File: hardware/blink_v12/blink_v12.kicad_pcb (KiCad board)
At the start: 2 copper layers, 119 x 92 mm, 176 parts, among them J1 Conn_01x02, J11 KH-BNC50-3511, J12 KH-BNC50-3511, J13 KH-BNC50-3511, J14 Conn_02x16_Odd_Even, J15 Conn_01x01, J16 Conn_01x01, J2 PJ-320D, J3 PJ-320D, J4 KH-BNC50-3511, J5 Conn_01x06_Pin, J6 Conn_01x03, J7 Conn_01x06_Pin, J9 USB_C_Receptacle, Q1 AO3400A, Q2 AO3400A, Q3 2N7002, Q4 2N7002, Q5 2N7002, SW1 SW_SPDT, SW2 SW_Push_4PDT, SW3 SW_Push_4PDT, SW4 SW_Push_4PDT, U1 AMS1117-3.3, U10 TMP112AIDRLR, U11 MAX40200AUK, U12 MAX40200AUK, U13 AMS1117-3.3, U14 SN74LVC1G14DBV, U15 BQ29702DSER, U16 TPS63060, U2 AD8397, U3 M24C02-RMN, U4 STM32F405RGTx, U5 SN74LVC1G14DBV, U6 SN74LVC1G14DBV, U7 CH340C, U8 USBLC6-2P6, U9 MCP73832-2-OT, X1 GTXO-14V (2.048MHz), Y1 16MHz

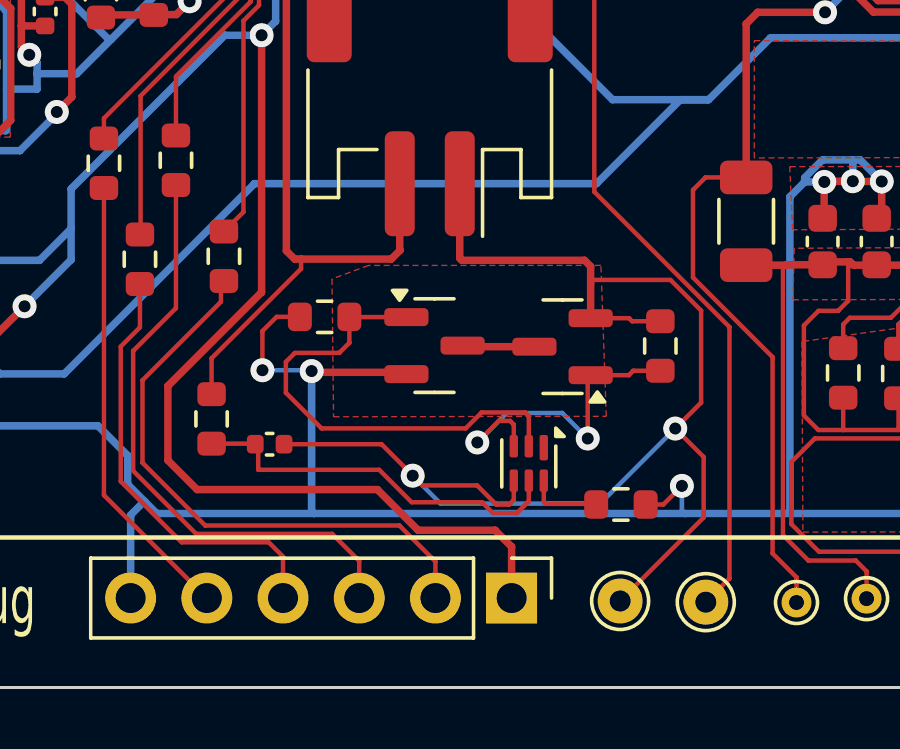
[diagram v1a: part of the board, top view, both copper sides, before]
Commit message: remove the battery protection circuit
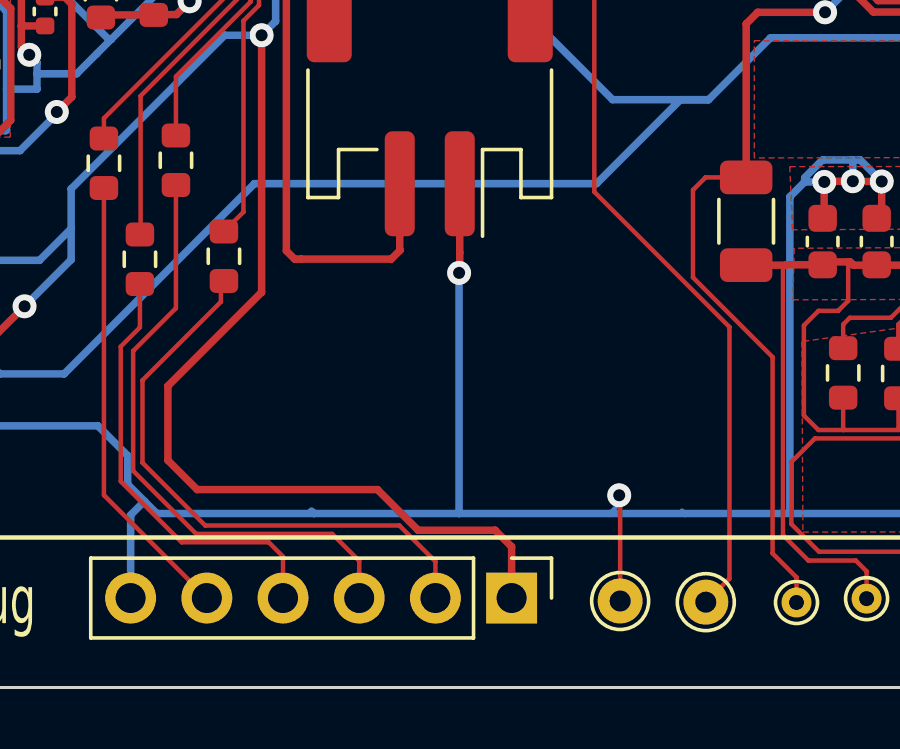
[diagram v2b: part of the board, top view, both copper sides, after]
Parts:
- removed C37: 100n, Capacitor_SMD:C_0402_1005Metric
- removed Q1, Q2: AO3400A, Package_TO_SOT_SMD:SOT-23
- removed R14: 330R, Resistor_SMD:R_0603_1608Metric
- removed R18: 2K2, Resistor_SMD:R_0603_1608Metric
- removed R34, R55: 2M0, Resistor_SMD:R_0603_1608Metric
- removed U15: BQ29702DSER, Package_SON:WSON-6_1.5x1.5mm_P0.5mm
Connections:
- J1 pad 1: Net-(J1-Pin_1) -> GND
- TP21 pad 1: Net-(J1-Pin_1) -> GND
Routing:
- net Net-(J1-Pin_1): track 46.1 -> 0.00 mm, vias 2 -> 0
- net Net-(Q1-G): track 16.0 -> 0.00 mm
- net Net-(U15-BAT): track 12.8 -> 0.00 mm
- net Net-(Q2-G): track 11.3 -> 0.00 mm, vias 2 -> 0
- net +BATT: track 157.8 -> 152.1 mm
- net Net-(U15-V-): track 2.48 -> 0.00 mm
- net /THERM1: track 2.41 -> 0.00 mm
- net GND: track 1200.3 -> 1201.0 mm, vias 62 -> 61
- removed copper zone on F.Cu, net /THERM1

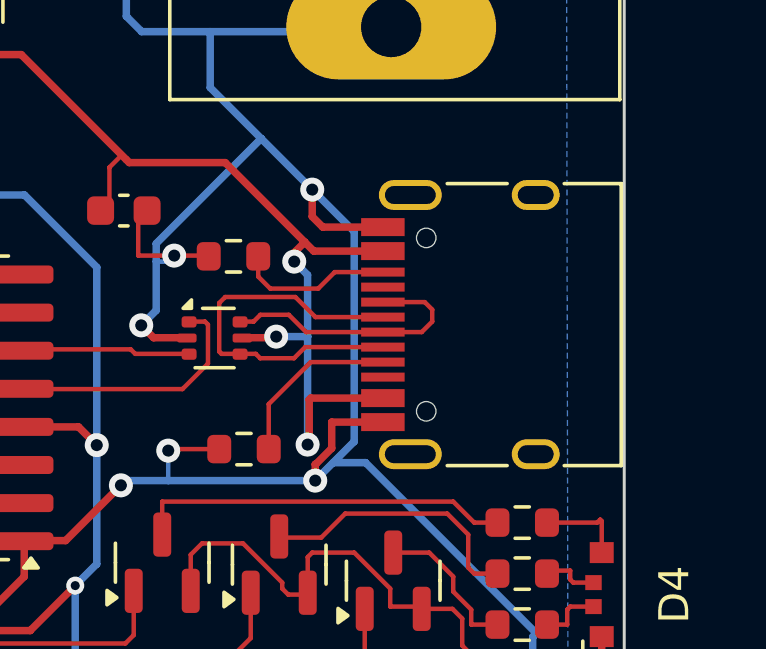
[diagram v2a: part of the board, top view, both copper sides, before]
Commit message: move USB connecro out 2 mm
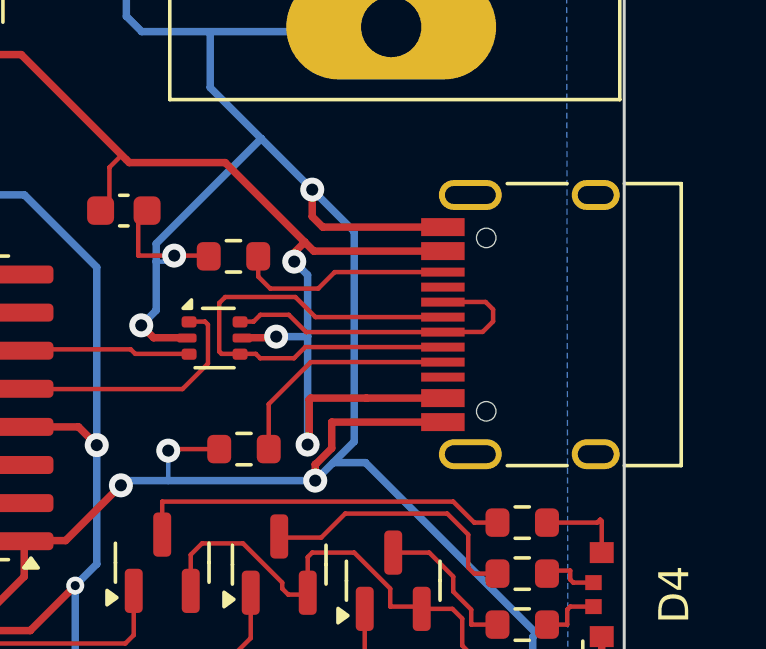
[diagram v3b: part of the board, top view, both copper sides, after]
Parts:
- moved J9 2.00 mm to (228.0, 66.0)
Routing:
- net GND: track 1201.0 -> 1205.0 mm
- net Net-(J9-D--PadA7): track 13.1 -> 17.1 mm
- net VBUS: track 143.3 -> 147.3 mm
- net Net-(J9-D+-PadA6): track 9.03 -> 11.0 mm
- net Net-(J9-CC2): track 5.22 -> 7.22 mm
- net Net-(J9-CC1): track 5.88 -> 7.88 mm

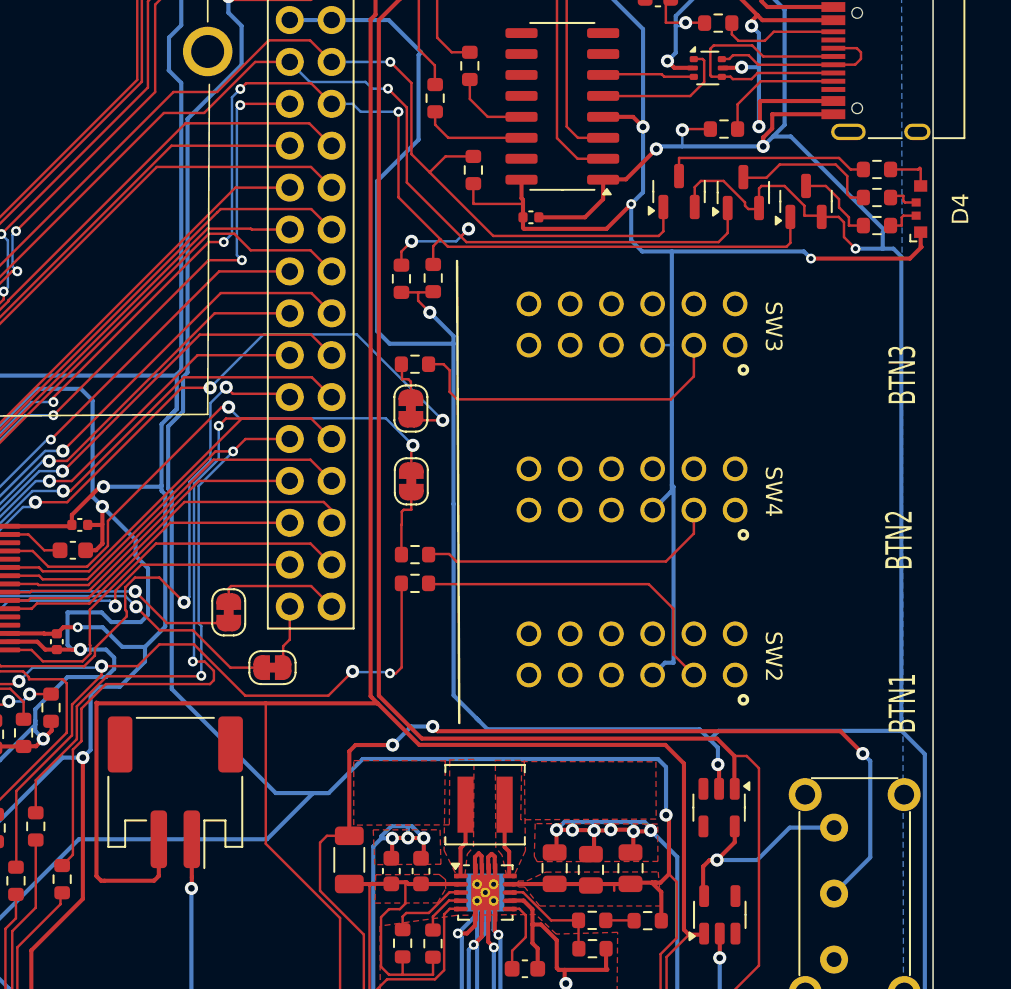
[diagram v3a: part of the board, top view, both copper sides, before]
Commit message: move LED over
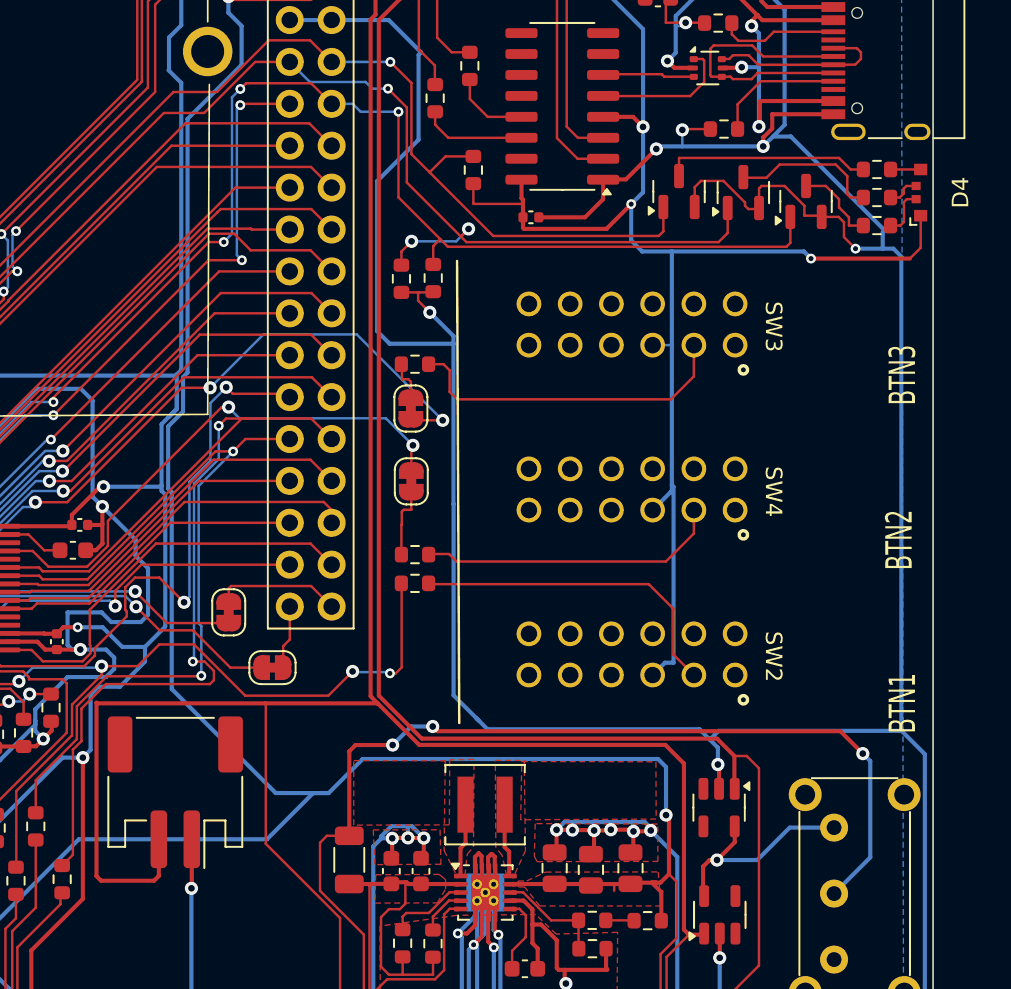
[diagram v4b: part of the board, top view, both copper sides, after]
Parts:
- moved D4 1.00 mm to (229.8, 74.0)
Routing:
- net Net-(D4-RK): track 2.94 -> 1.82 mm
- net +3.3V: track 504.9 -> 505.8 mm
- net Net-(D4-BK): track 2.09 -> 2.94 mm
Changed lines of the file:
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@@
 		(locked yes)
 		(layer "F.Cu")
-		(at 229.8 75 90)
+		(at 229.8 74 90)
 		(descr "LED, RGB, right-angle, clear, https://everlightamericas.com/index.php?controller=attachment&id_attachment=3220")
 		(tags "LED RGB right-angle")
@@
 	)
 	(segment
-		(start 229.3 77.3)
-		(end 229.25 77.25)
-		(width 0.25)
-		(layer "F.Cu")
-		(net 1)
-	)
-	(segment
 		(start 188.485027 60.827484)
 		(end 188.657543 61)
@@
 	)
 	(segment
+		(start 229.25 75.4)
+		(end 229.25 77.35)
+		(width 0.15)
+		(layer "F.Cu")
+		(net 1)
+	)
+	(segment
 		(start 195.130562 47.911232)
 		(end 195.67984 47.361954)
@@
 	)
 	(segment
-		(start 229.25 77.25)
-		(end 229.25 76.4)
-		(width 0.25)
-		(layer "F.Cu")
-		(net 1)
-	)
-	(segment
 		(start 138.66596 52.2911)
 		(end 138.66596 50.742973)
@@
 	)
 	(segment
-		(start 228.6 78)
-		(end 229.3 77.3)
-		(width 0.25)
-		(layer "F.Cu")
-		(net 1)
-	)
-	(segment
 		(start 173.888472 94.228212)
 		(end 177.709429 94.228212)
@@
 	)
 	(segment
+		(start 229.25 77.35)
+		(end 228.6 78)
+		(width 0.15)
+		(layer "F.Cu")
+		(net 1)
+	)
+	(segment
 		(start 137.166041 52.752614)
 		(end 138.204446 52.752614)
@@
 	(segment
 		(start 185.060701 113.208027)
-		(end 185.060701 115.503917)
+		(end 185.060701 116.157776)
 		(width 0.25)
 		(layer "F.Cu")
@@
 	)
 	(segment
-		(start 185.060701 115.503917)
-		(end 185.060701 116.157776)
-		(width 0.25)
-		(layer "F.Cu")
-		(net 21)
-	)
-	(segment
 		(start 141.313312 57.888081)
 		(end 142.34286 57.888081)
@@
 	)
 	(segment
-		(start 221.405646 68.45)
-		(end 223.955 68.45)
-		(width 0.25)
-		(layer "F.Cu")
-		(net 78)
-	)
-	(segment
 		(start 202.812665 57)
 		(end 201.8 57)
@@
 	)
 	(segment
-		(start 221.405646 68.45)
-		(end 219.55 68.45)
+		(start 219.55 68.45)
+		(end 223.955 68.45)
 		(width 0.25)
 		(layer "F.Cu")
@@
 	(segment
 		(start 179.557365 115.719292)
-		(end 179.771445 115.719292)
+		(end 182.777179 115.719292)
 		(width 0.25)
 		(layer "F.Cu")
@@
 	)
 	(segment
-		(start 179.771445 115.719292)
-		(end 182.777179 115.719292)
-		(width 0.25)
-		(layer "F.Cu")
-		(net 79)
-	)
-	(segment
 		(start 194.051054 126.36611)
 		(end 193.262239 127.154925)
@@
 	)
 	(segment
-		(start 228.2 75.4)
-		(end 228.975 75.4)
+		(start 228.236214 75.78924)
+		(end 228.011906 76.013548)
 		(width 0.15)
 		(layer "F.Cu")
@@
 	)
 	(segment
-		(start 228.1 76)
-		(end 228.1 75.5)
+		(start 228.975 74.4)
+		(end 228.409465 74.4)
 		(width 0.15)
 		(layer "F.Cu")
@@
 	)
 	(segment
-		(start 228.1 75.5)
-		(end 228.2 75.4)
+		(start 227.998358 76)
+		(end 227.425 76)
 		(width 0.15)
 		(layer "F.Cu")
@@
 	)
 	(segment
-		(start 227.425 76)
-		(end 228.1 76)
+		(start 228.011906 76.013548)
+		(end 227.998358 76)
 		(width 0.15)
 		(layer "F.Cu")
@@
 	)
 	(segment
-		(start 228.2 74.5)
-		(end 228.2 74.2)
+		(start 228.409465 74.4)
+		(end 228.236214 74.573251)
 		(width 0.15)
 		(layer "F.Cu")
-		(net 116)
+		(net 115)
 	)
 	(segment
-		(start 228.3 74.6)
-		(end 228.2 74.5)
+		(start 228.236214 74.573251)
+		(end 228.236214 75.78924)
 		(width 0.15)
 		(layer "F.Cu")
-		(net 116)
+		(net 115)
 	)
 	(segment
-		(start 228.2 74.2)
-		(end 227.525 74.2)
+		(start 228.382499 73.6)
+		(end 228.975 73.6)
 		(width 0.15)
 		(layer "F.Cu")
@@
 	)
 	(segment
-		(start 228.975 74.6)
-		(end 228.3 74.6)
+		(start 227.425 74.3)
+		(end 227.984112 74.3)
 		(width 0.15)
 		(layer "F.Cu")
@@
 	)
 	(segment
-		(start 229.25 72.55)
-		(end 229.2 72.5)
+		(start 227.984112 74.3)
+		(end 228.224409 74.059703)
 		(width 0.15)
 		(layer "F.Cu")
-		(net 117)
+		(net 116)
 	)
 	(segment
-		(start 229.25 73.6)
-		(end 229.25 72.55)
+		(start 228.224409 73.75809)
+		(end 228.382499 73.6)
 		(width 0.15)
 		(layer "F.Cu")
-		(net 117)
+		(net 116)
 	)
 	(segment
-		(start 229.2 72.5)
-		(end 229.1 72.6)
+		(start 228.224409 74.059703)
+		(end 228.224409 73.75809)
 		(width 0.15)
 		(layer "F.Cu")
-		(net 117)
+		(net 116)
 	)
 	(segment
-		(start 229.1 72.6)
+		(start 229.25 72.6)
 		(end 227.425 72.6)
 		(width 0.15)

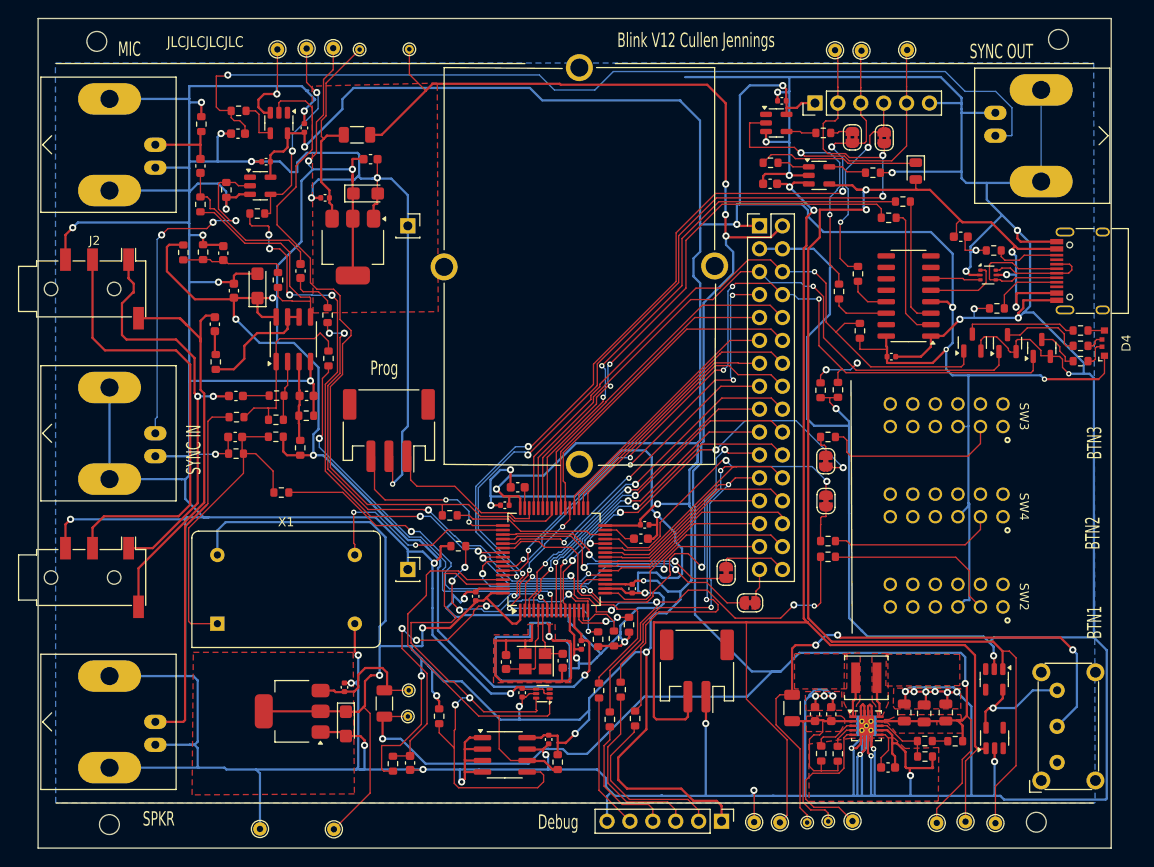
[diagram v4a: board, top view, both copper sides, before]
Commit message: moved the test points off rails
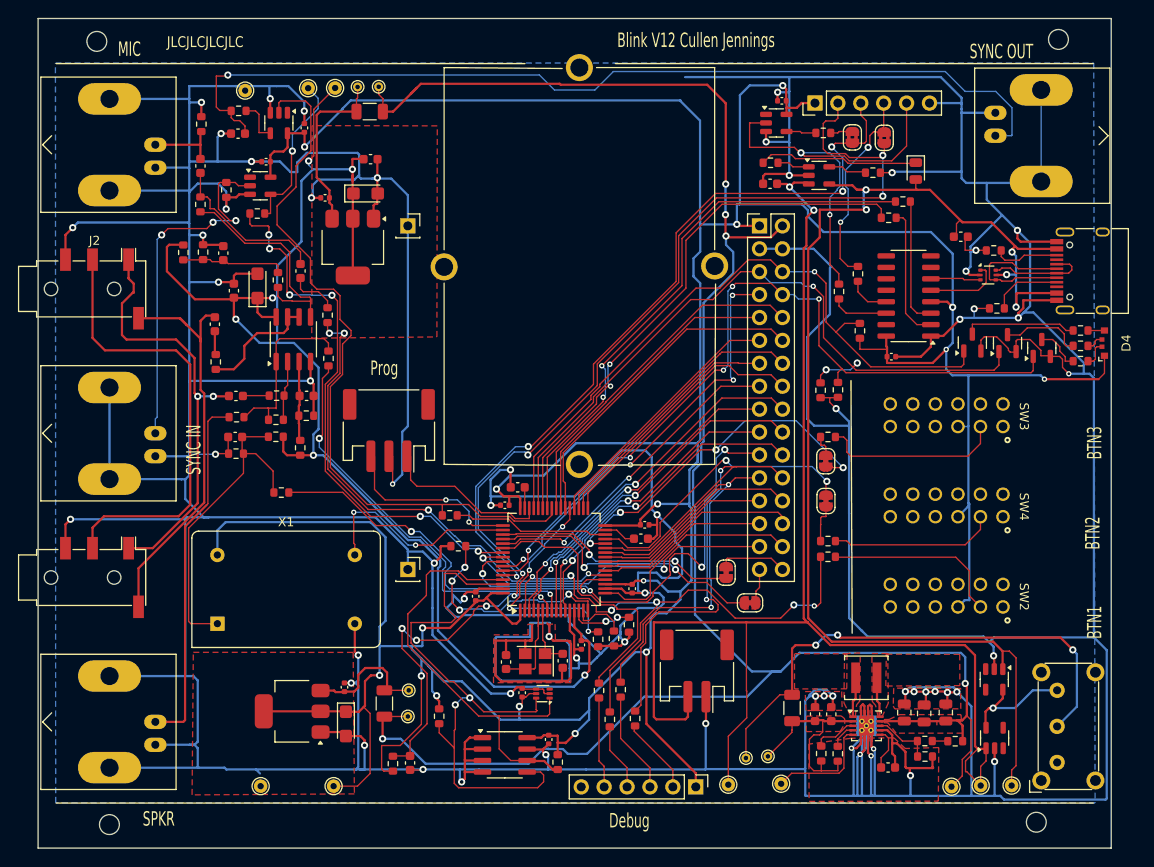
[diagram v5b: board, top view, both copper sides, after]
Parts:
- removed TP21, TP6, TP7, TP8: ~, TestPoint:TestPoint_THTPad_D1.5mm_Drill0.7mm
- moved TP12 9.87 mm to (189.5, 120.0)
- moved TP13 9.84 mm to (191.9, 119.8)
- moved TP10 8.93 mm to (193.4, 122.9)
- moved TP20 7.09 mm to (187.5, 123.0)
- moved TP14 5.80 mm to (134.0, 46.0)
- moved TP1 5.37 mm to (148.8, 45.6)
- moved TP15 4.79 mm to (143.8, 123.1)
- moved J7 4.76 mm to (183.9, 123.2)
- moved TP9 4.75 mm to (135.7, 123.1)
- moved TP16 4.54 mm to (219.0, 123.1)
- moved TP18 4.42 mm to (143.9, 45.7)
- moved TP5 4.41 mm to (140.9, 45.7)
- moved TP11 4.34 mm to (212.3, 123.2)
- moved TP17 4.33 mm to (215.5, 123.1)
- moved TP2 4.15 mm to (146.4, 45.6)
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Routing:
- net GND: track 1205.0 -> 1177.8 mm, vias 61 -> 60
- net +3.3V: track 505.8 -> 488.2 mm
- net Net-(J7-Pin_2): track 19.5 -> 8.59 mm
- net Net-(J7-Pin_3): track 20.1 -> 11.3 mm
- net +4V: track 235.7 -> 227.1 mm
- net /VIN1: track 31.6 -> 23.4 mm
- net Net-(J7-Pin_4): track 14.7 -> 7.45 mm
- net Net-(SW1-B): track 64.3 -> 57.1 mm
- net /USB_RTS: track 52.9 -> 47.1 mm
- net /BOOT0: track 92.2 -> 86.5 mm
- net /NRST: track 141.0 -> 135.5 mm
- net Net-(U16-PG): track 17.3 -> 11.9 mm
- net Net-(J7-Pin_5): track 15.1 -> 10.1 mm
- net VBUS: track 147.3 -> 142.4 mm
- net Net-(R28-Pad2): track 22.4 -> 18.0 mm, vias 2 -> 1
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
